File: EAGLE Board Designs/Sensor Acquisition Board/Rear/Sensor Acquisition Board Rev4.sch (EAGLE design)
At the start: 38 parts, among them J1 CONNECTOR-SENSOR_NF_S_RA_BLACK, J10 JUMPER_1X02_, J2 CONNECTOR-SENSOR_NF_S_RA_BLACK, J3 CONNECTOR-SENSOR_NF_S_RA_BLACK, J4 CONNECTOR-SENSOR_NF_S_RA_BLACK, J5 CONNECTOR-SENSOR_NF_S_RA_BLACK, J6 CONNECTOR-SENSOR_NF_S_RA_BLACK, J7 CONNECTOR-SENSOR_NF_S_RA_BLACK, J8 CONNECTOR-SENSOR_NF_S_RA_BLACK, J9 CONNECTOR-CAN_NF_S_RA_BLACK, U1 VOLTAGE_REGULATOR_SOT223_5V, U3 TCAN1051HQV-Q1

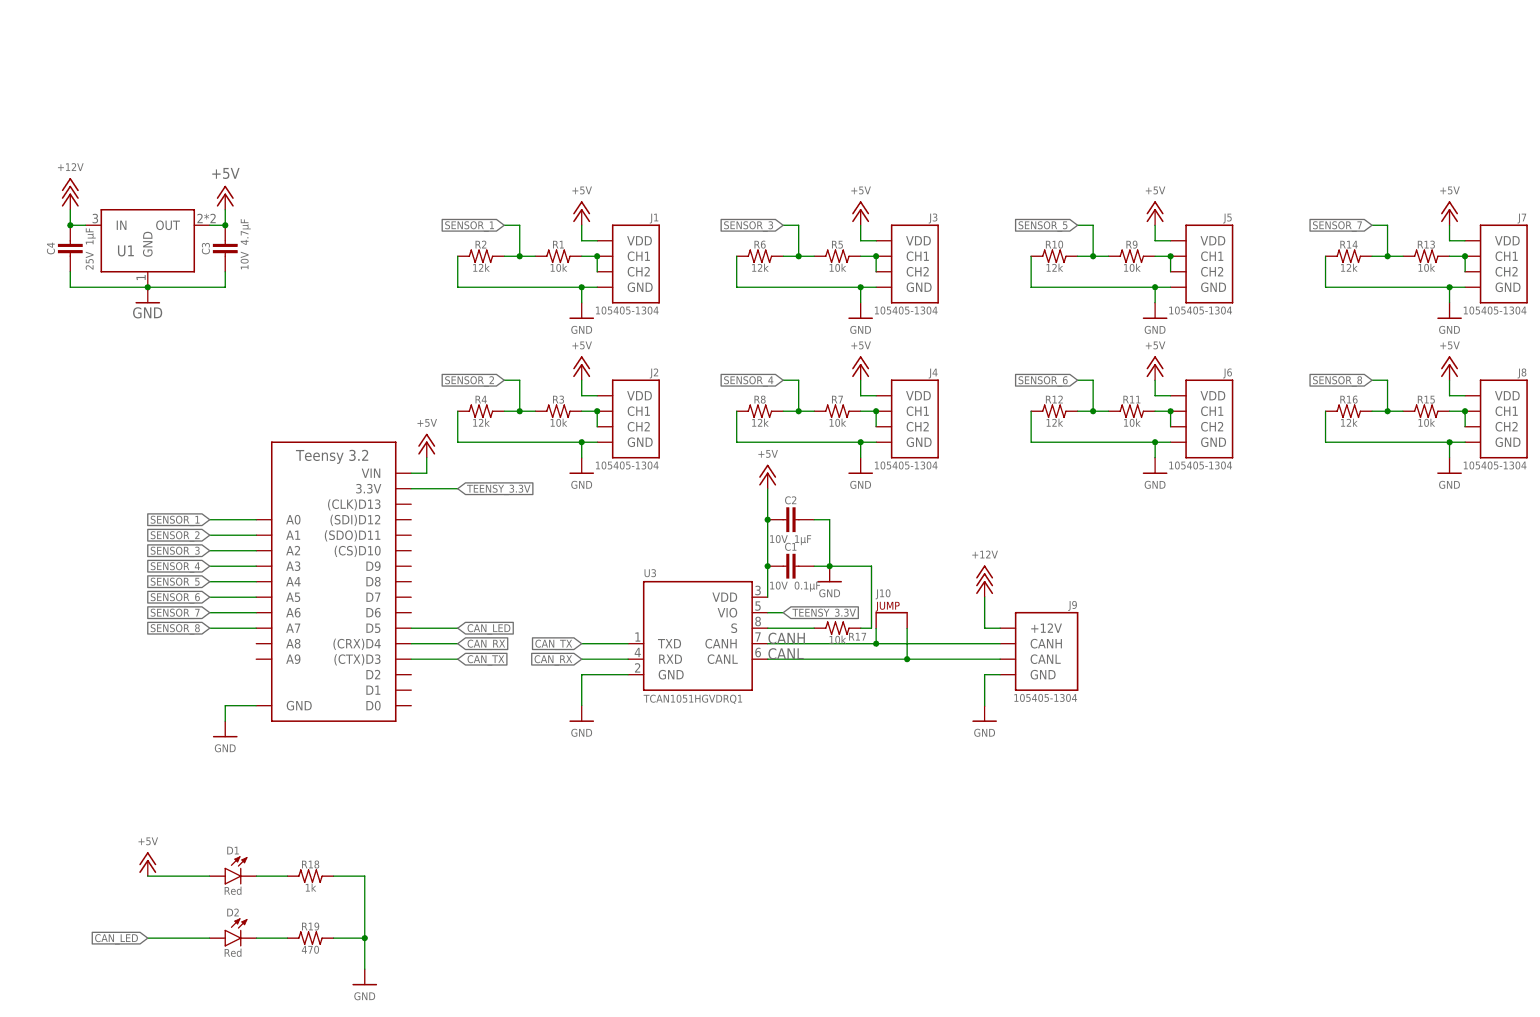
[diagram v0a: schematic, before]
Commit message: Started on rear board sch
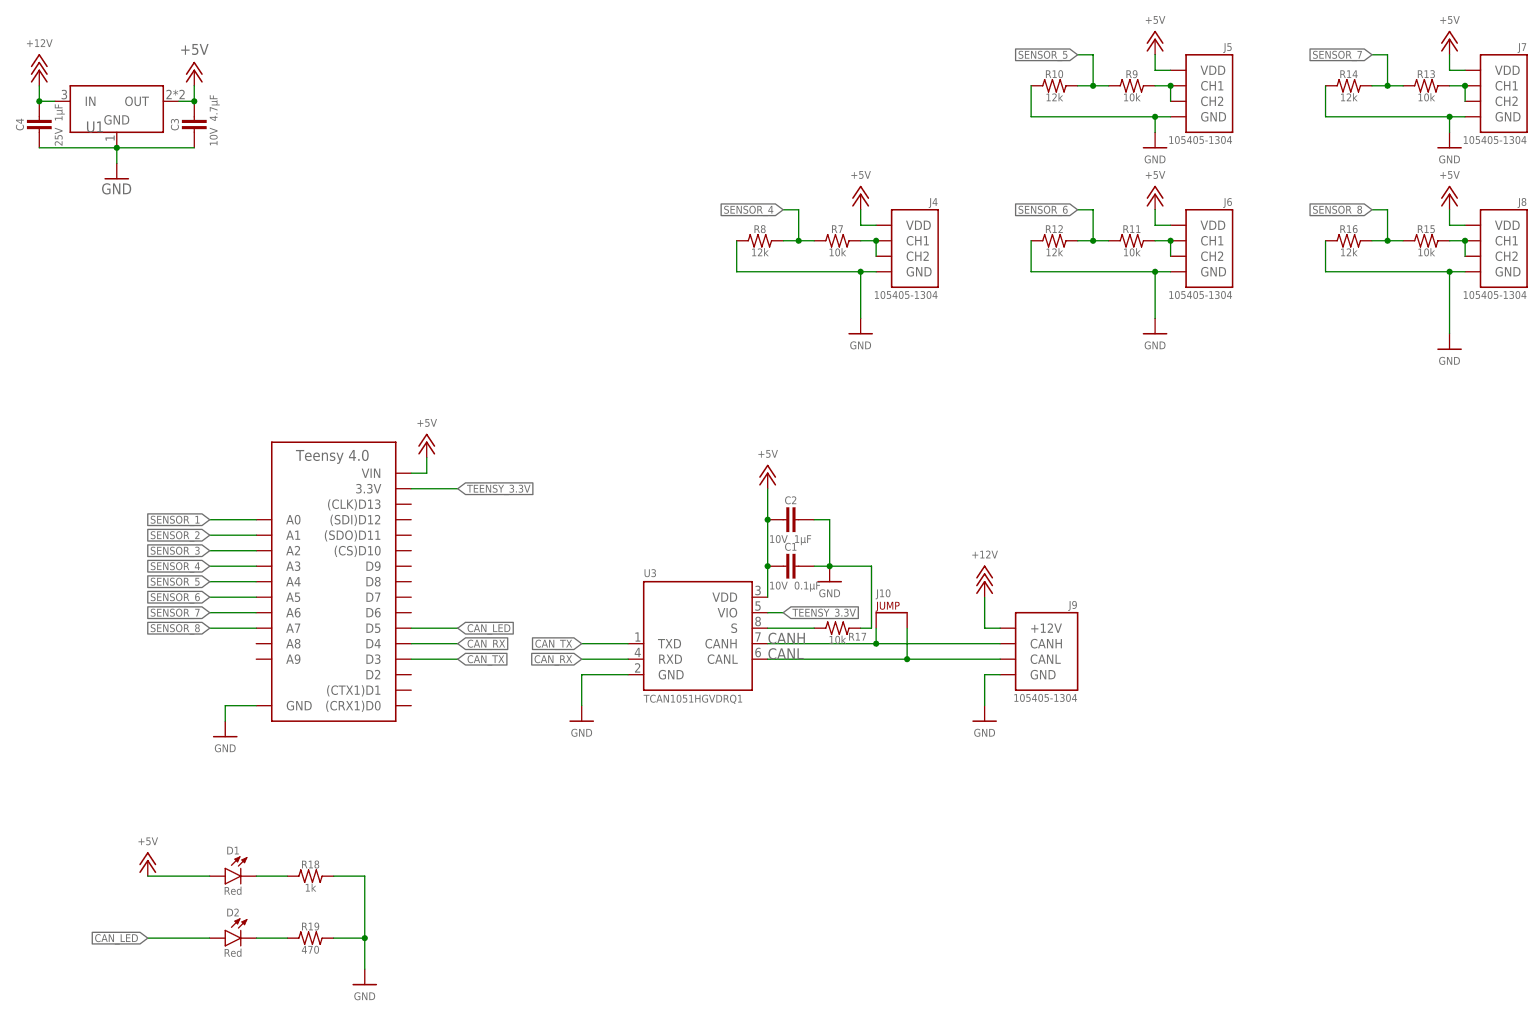
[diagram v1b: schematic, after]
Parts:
- removed A1: TEENSY_3.2, HyTechDevices:TEENSY_3.2
- removed J1, J2, J3: CONNECTOR-SENSOR_NF_S_RA_BLACK, HyTechDevices:CONNECTOR-SENSOR_NF_S_RA_BLACK
- removed R1, R3, R5: RESISTOR_0603_10K, HyTechDevices:RESISTOR_0603_10K
- removed R2, R4, R6: RESISTOR_0603_12K, HyTechDevices:RESISTOR_0603_12K
- added A2: TEENSY_4.0, HyTechDevices:TEENSY_4.0
- J10: value JUMPER_1X02_ -> JUMPER_0603_; device HyTechDevices:JUMPER_1X02_ -> HyTechDevices:JUMPER_0603_
- U1: value VOLTAGE_REGULATOR_SOT223_5V -> VOLTAGE_REGULATOR_SOT-223_5V; device HyTechDevices:VOLTAGE_REGULATOR_SOT223_5V -> HyTechDevices:VOLTAGE_REGULATOR_SOT-223_5V
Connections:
- removed net N$10: J2.CH1, J2.CH2, R3.2
- removed net N$11: J3.CH1, J3.CH2, R5.2
- removed net N$8: J1.CH1, J1.CH2, R1.2
- net +5V: now also A2.VIN; no longer A1.VIN, J1.VDD, J2.VDD, J3.VDD
- net CANH: now also J10.1; no longer J10.P$1
- net CANL: now also J10.2; no longer J10.P$2
- net CAN_LED: now also A2.D5; no longer A1.D5
- net CAN_RX: now also A2.D4; no longer A1.(CRX)D4
- net CAN_TX: now also A2.D3; no longer A1.(CTX)D3
- net GND: now also A2.GND; no longer A1.GND, J1.GND, J2.GND, J3.GND, R2.1, R4.1, R6.1
- net SENSOR_1: now also A2.A0; no longer A1.A0, R1.1, R2.2
- net SENSOR_2: now also A2.A1; no longer A1.A1, R3.1, R4.2
- net SENSOR_3: now also A2.A2; no longer A1.A2, R5.1, R6.2
- net SENSOR_4: now also A2.A3; no longer A1.A3
- net SENSOR_5: now also A2.A4; no longer A1.A4
- net SENSOR_6: now also A2.A5; no longer A1.A5
- net SENSOR_7: now also A2.A6; no longer A1.A6
- net SENSOR_8: now also A2.A7; no longer A1.A7
- net TEENSY_3.3V: now also A2.3.3V; no longer A1.3.3V
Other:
- moved on the sheet: C3, C4, J4, J5, J6, J7, J8, R10, R11, R12, R13, R14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
